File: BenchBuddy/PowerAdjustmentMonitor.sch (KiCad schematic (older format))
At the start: 0 parts

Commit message: Week3 Part 2
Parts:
- added JP? (x3): JUMPER, ~, symbol JUMPER
- added R? (x8): R, ~, symbol R
- added R? (x2): RVAR, ~, symbol RVAR
- added U? (x2): LM317, ~, symbol LM317
- added U? (x2): 7805, ~, symbol 7805
- added U? (x2): LM324, symbol LM324
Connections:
- new net: R?.1, R?.2, U?.2 (ADJ)
- new net: R?.2, R?.2, U?.2 (ADJ)
- new net +12V: U?.1 (IN), U?.4 (V+), U?.4 (V+), U?.VI
- new net -12V: JP?.2, U?.1 (IN), U?.11 (V-), U?.11 (V-), U?.VI
- new net AGND: JP?.2, R?.1, R?.1, R?.1, R?.2, U?.GND, U?.GND
- new net FE_V+: JP?.2, U?.VO
- new net FE_V-: JP?.1, U?.VO
- new net GND: JP?.1
- new net V+_ADJ: R?.1, R?.2
- new net V+_ADJ_MON: R?.1, R?.2
- new net V+_CURR_MON: U?.1, U?.2 (-)
- new net V+_MON: R?.1, R?.1, U?.3 (+), U?.3 (OUT)
- new net V-_ADJ: R?.2, R?.2
- new net V-_ADJ_MON: R?.1, R?.2
- new net V-_CURR_MON: U?.1, U?.2 (-)
- new net V-_MON: R?.1, R?.2, U?.3 (+), U?.3 (OUT)

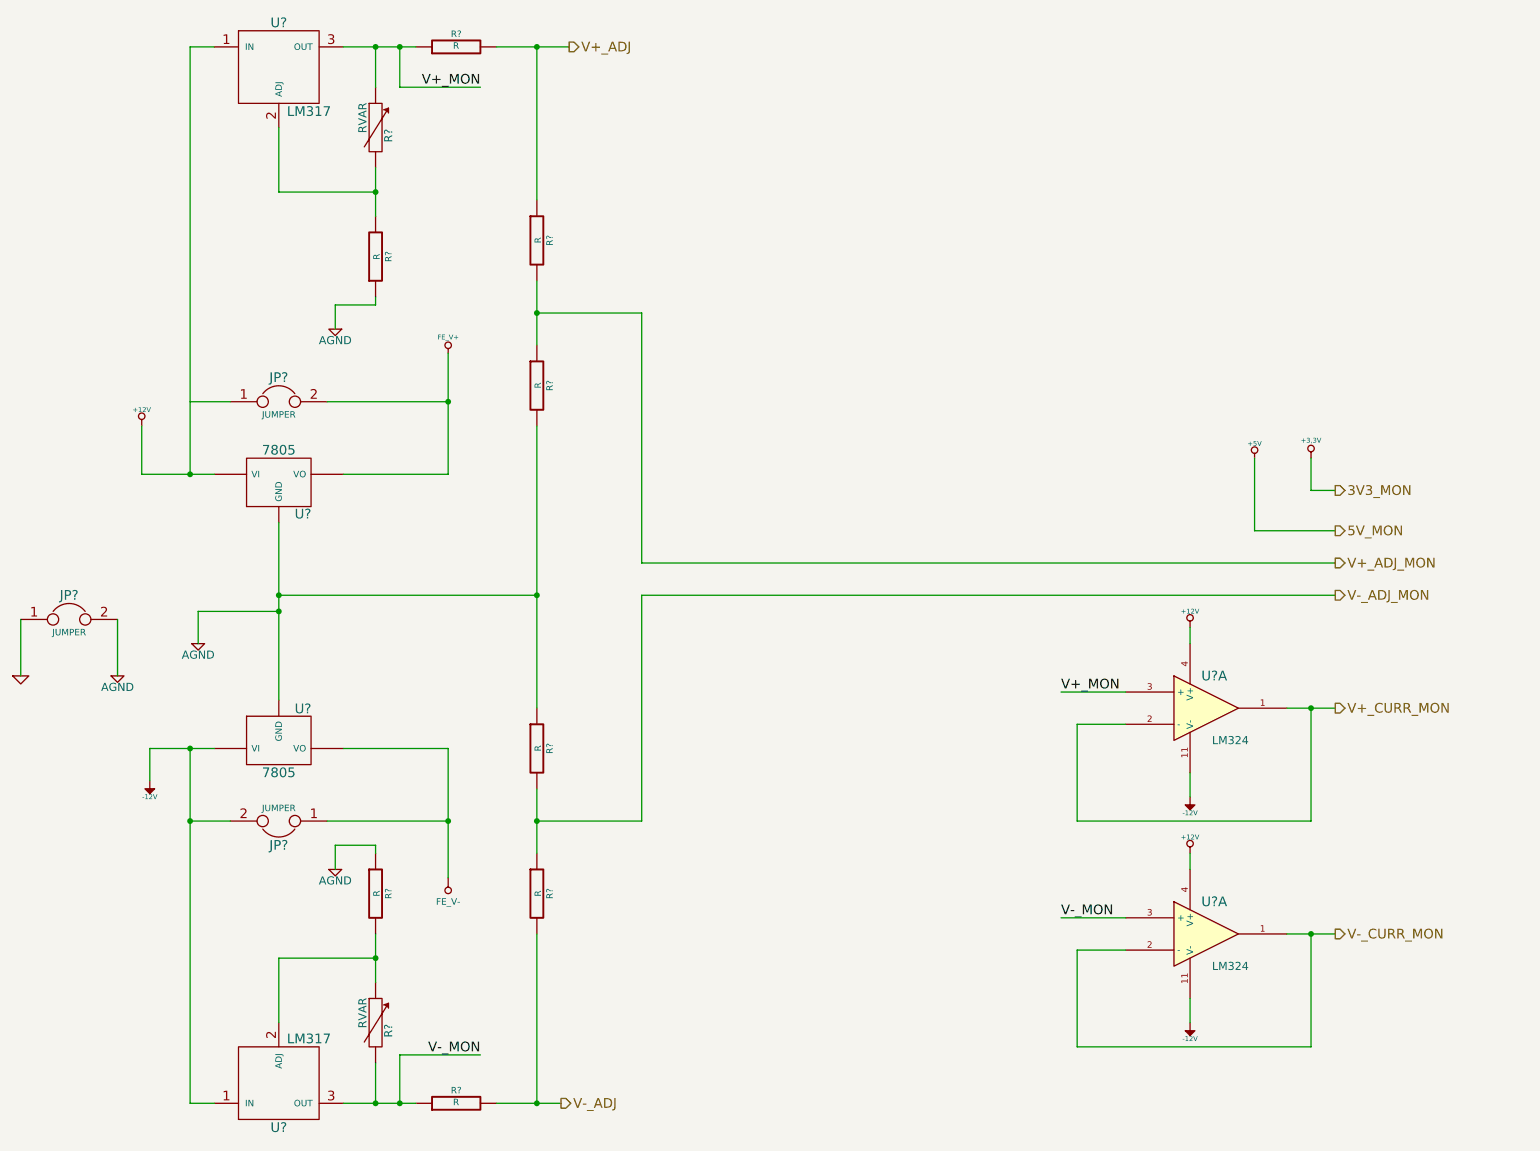
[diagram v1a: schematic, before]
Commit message: Colocação dos Componentes Relé
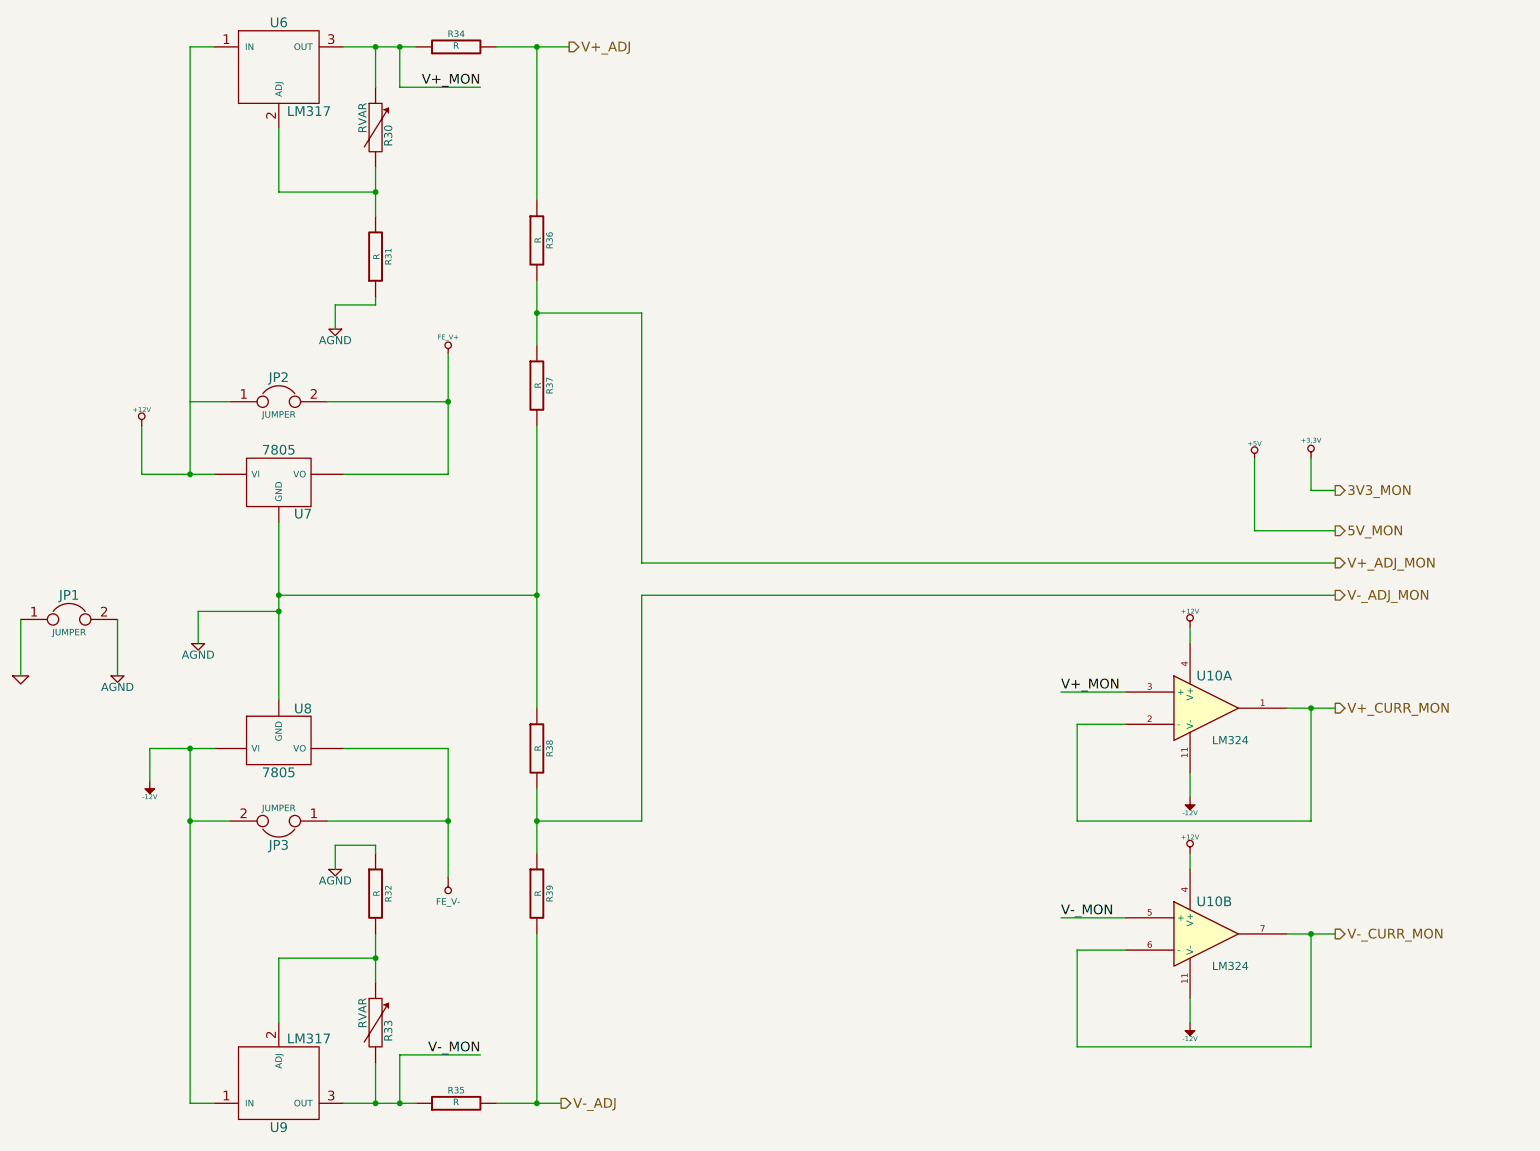
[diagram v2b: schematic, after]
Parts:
- gave numbers to parts that had none: 18
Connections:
- net V-_CURR_MON: now also U10.6 (-), U10.7; no longer U10.1, U10.2 (-)
- net V-_MON: now also U10.5 (+); no longer U10.3 (+)
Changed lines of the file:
@@
 Sheet 6 9
 Title ""
-Date "7 mar 2014"
+Date "9 mar 2014"
 Rev ""
 Comp ""
@@
 $EndDescr
 $Comp
-L +3,3V #PWR?
+L +3,3V #PWR44
 U 1 1 531776F8
 P 9050 3500
-F 0 "#PWR?" H 9050 3460 30  0001 C CNN
+F 0 "#PWR44" H 9050 3460 30  0001 C CNN
 F 1 "+3,3V" H 9050 3610 30  0000 C CNN
 F 2 "" H 9050 3500 60  0000 C CNN
@@
 $EndComp
 $Comp
-L +5V #PWR?
+L +5V #PWR43
 U 1 1 531776FE
 P 8700 3500
-F 0 "#PWR?" H 8700 3590 20  0001 C CNN
+F 0 "#PWR43" H 8700 3590 20  0001 C CNN
 F 1 "+5V" H 8700 3590 30  0000 C CNN
 F 2 "" H 8700 3500 60  0000 C CNN
@@
 $EndComp
 $Comp
-L +12V #PWR?
+L +12V #PWR32
 U 1 1 5317778A
 P 1800 3300
-F 0 "#PWR?" H 1800 3250 20  0001 C CNN
+F 0 "#PWR32" H 1800 3250 20  0001 C CNN
 F 1 "+12V" H 1800 3400 30  0000 C CNN
 F 2 "" H 1800 3300 60  0000 C CNN
@@
 $EndComp
 $Comp
-L -12V #PWR?
+L -12V #PWR33
 U 1 1 53177790
 P 1850 5500
-F 0 "#PWR?" H 1850 5630 20  0001 C CNN
+F 0 "#PWR33" H 1850 5630 20  0001 C CNN
 F 1 "-12V" H 1850 5600 30  0000 C CNN
 F 2 "" H 1850 5500 60  0000 C CNN
@@
 $EndComp
 $Comp
-L LM317 U?
+L LM317 U9
 U 1 1 531777B3
 P 2650 7350
-F 0 "U?" H 2650 7650 60  0000 C CNN
+F 0 "U9" H 2650 7650 60  0000 C CNN
 F 1 "LM317" H 2700 7100 60  0000 L CNN
 F 2 "~" H 2650 7350 60  0000 C CNN
@@
 	1850 5300 1850 5500
 $Comp
-L JUMPER JP?
+L JUMPER JP2
 U 1 1 531777D1
 P 2650 3150
-F 0 "JP?" H 2650 3300 60  0000 C CNN
+F 0 "JP2" H 2650 3300 60  0000 C CNN
 F 1 "JUMPER" H 2650 3070 40  0000 C CNN
 F 2 "~" H 2650 3150 60  0000 C CNN
@@
 $EndComp
 $Comp
-L JUMPER JP?
+L JUMPER JP3
 U 1 1 531777DE
 P 2650 5750
-F 0 "JP?" H 2650 5900 60  0000 C CNN
+F 0 "JP3" H 2650 5900 60  0000 C CNN
 F 1 "JUMPER" H 2650 5670 40  0000 C CNN
 F 2 "~" H 2650 5750 60  0000 C CNN
@@
 Connection ~ 2650 4450
 $Comp
-L JUMPER JP?
+L JUMPER JP1
 U 1 1 53177825
 P 1350 4500
-F 0 "JP?" H 1350 4650 60  0000 C CNN
+F 0 "JP1" H 1350 4650 60  0000 C CNN
 F 1 "JUMPER" H 1350 4420 40  0000 C CNN
 F 2 "~" H 1350 4500 60  0000 C CNN
@@
 $EndComp
 $Comp
-L AGND #PWR?
+L AGND #PWR31
 U 1 1 5317782D
 P 1650 4850
-F 0 "#PWR?" H 1650 4850 40  0001 C CNN
+F 0 "#PWR31" H 1650 4850 40  0001 C CNN
 F 1 "AGND" H 1650 4780 50  0000 C CNN
 F 2 "~" H 1650 4850 60  0000 C CNN
@@
 $EndComp
 $Comp
-L GND #PWR?
+L GND #PWR30
 U 1 1 5317783C
 P 1050 4850
-F 0 "#PWR?" H 1050 4850 30  0001 C CNN
+F 0 "#PWR30" H 1050 4850 30  0001 C CNN
 F 1 "GND" H 1050 4780 30  0001 C CNN
 F 2 "~" H 1050 4850 60  0000 C CNN
@@
 	1650 4500 1650 4850
 $Comp
-L AGND #PWR?
+L AGND #PWR34
 U 1 1 53177892
 P 2150 4650
-F 0 "#PWR?" H 2150 4650 40  0001 C CNN
+F 0 "#PWR34" H 2150 4650 40  0001 C CNN
 F 1 "AGND" H 2150 4580 50  0000 C CNN
 F 2 "~" H 2150 4650 60  0000 C CNN
@@
 $EndComp
 $Comp
-L FE_V+ #PWR?
+L FE_V+ #PWR37
 U 1 1 53177BD8
 P 3700 2850
-F 0 "#PWR?" H 3700 2950 30  0001 C CNN
+F 0 "#PWR37" H 3700 2950 30  0001 C CNN
 F 1 "FE_V+" H 3700 2950 30  0000 C CNN
 F 2 "~" H 3700 2850 60  0000 C CNN
@@
 $EndComp
 $Comp
-L FE_V- #PWR?
+L FE_V- #PWR38
 U 1 1 53177BE7
 P 3700 6100
-F 0 "#PWR?" H 3700 6300 40  0001 C CNN
+F 0 "#PWR38" H 3700 6300 40  0001 C CNN
 F 1 "FE_V-" H 3700 6250 40  0000 C CNN
 F 2 "~" H 3700 6100 60  0000 C CNN
@@
 $EndComp
 $Comp
-L 7805 U?
+L 7805 U7
 U 1 1 53177C4D
 P 2650 3650
-F 0 "U?" H 2800 3454 60  0000 C CNN
+F 0 "U7" H 2800 3454 60  0000 C CNN
 F 1 "7805" H 2650 3850 60  0000 C CNN
 F 2 "~" H 2650 3650 60  0000 C CNN
@@
 $EndComp
 $Comp
-L 7805 U?
+L 7805 U8
 U 1 1 53177C64
 P 2650 5250
-F 0 "U?" H 2800 5054 60  0000 C CNN
+F 0 "U8" H 2800 5054 60  0000 C CNN
 F 1 "7805" H 2650 5450 60  0000 C CNN
 F 2 "~" H 2650 5250 60  0000 C CNN
@@
 Connection ~ 3700 5750
 $Comp
-L R R?
+L R R32
 U 1 1 53177DDD
 P 3250 6200
-F 0 "R?" V 3330 6200 40  0000 C CNN
+F 0 "R32" V 3330 6200 40  0000 C CNN
 F 1 "R" V 3257 6201 40  0000 C CNN
 F 2 "~" V 3180 6200 30  0000 C CNN
@@
 Connection ~ 3250 6600
 $Comp
-L AGND #PWR?
+L AGND #PWR36
 U 1 1 53177E7E
 P 3000 6050
-F 0 "#PWR?" H 3000 6050 40  0001 C CNN
+F 0 "#PWR36" H 3000 6050 40  0001 C CNN
 F 1 "AGND" H 3000 5980 50  0000 C CNN
 F 2 "~" H 3000 6050 60  0000 C CNN
@@
 	3000 5900 3000 6050
 $Comp
-L LM317 U?
+L LM317 U6
 U 1 1 53177EB1
 P 2650 1100
-F 0 "U?" H 2650 1400 60  0000 C CNN
+F 0 "U6" H 2650 1400 60  0000 C CNN
 F 1 "LM317" H 2700 850 60  0000 L CNN
 F 2 "~" H 2650 1100 60  0000 C CNN
@@
 	2100 950  2250 950
 $Comp
-L R R?
+L R R31
 U 1 1 53177EBF
 P 3250 2250
-F 0 "R?" V 3330 2250 40  0000 C CNN
+F 0 "R31" V 3330 2250 40  0000 C CNN
 F 1 "R" V 3257 2251 40  0000 C CNN
 F 2 "~" V 3180 2250 30  0000 C CNN
@@
 Connection ~ 3250 1850
 $Comp
-L AGND #PWR?
+L AGND #PWR35
 U 1 1 53177ECC
 P 3000 2700
-F 0 "#PWR?" H 3000 2700 40  0001 C CNN
+F 0 "#PWR35" H 3000 2700 40  0001 C CNN
 F 1 "AGND" H 3000 2630 50  0000 C CNN
 F 2 "~" H 3000 2700 60  0000 C CNN
@@
 V-_CURR_MON
 $Comp
-L R R?
+L R R36
 U 1 1 53178157
 P 4250 2150
-F 0 "R?" V 4330 2150 40  0000 C CNN
+F 0 "R36" V 4330 2150 40  0000 C CNN
 F 1 "R" V 4257 2151 40  0000 C CNN
 F 2 "~" V 4180 2150 30  0000 C CNN
@@
 $EndComp
 $Comp
-L R R?
+L R R37
 U 1 1 53178166
 P 4250 3050
-F 0 "R?" V 4330 3050 40  0000 C CNN
+F 0 "R37" V 4330 3050 40  0000 C CNN
 F 1 "R" V 4257 3051 40  0000 C CNN
 F 2 "~" V 4180 3050 30  0000 C CNN
@@
 Connection ~ 2650 4350
 $Comp
-L R R?
+L R R38
 U 1 1 5317820A
 P 4250 5300
-F 0 "R?" V 4330 5300 40  0000 C CNN
+F 0 "R38" V 4330 5300 40  0000 C CNN
 F 1 "R" V 4257 5301 40  0000 C CNN
 F 2 "~" V 4180 5300 30  0000 C CNN
@@
 $EndComp
 $Comp
-L R R?
+L R R39
 U 1 1 53178210
 P 4250 6200
-F 0 "R?" V 4330 6200 40  0000 C CNN
+F 0 "R39" V 4330 6200 40  0000 C CNN
 F 1 "R" V 4257 6201 40  0000 C CNN
 F 2 "~" V 4180 6200 30  0000 C CNN
@@
 	9050 3700 9200 3700
 $Comp
-L R R?
+L R R35
 U 1 1 531783D8
 P 3750 7500
-F 0 "R?" V 3830 7500 40  0000 C CNN
+F 0 "R35" V 3830 7500 40  0000 C CNN
 F 1 "R" V 3757 7501 40  0000 C CNN
 F 2 "~" V 3680 7500 30  0000 C CNN
@@
 $EndComp
 $Comp
-L R R?
+L R R34
 U 1 1 531783DE
 P 3750 950
-F 0 "R?" V 3830 950 40  0000 C CNN
+F 0 "R34" V 3830 950 40  0000 C CNN
 F 1 "R" V 3757 951 40  0000 C CNN
 F 2 "~" V 3680 950 30  0000 C CNN
@@
 	4900 2600 4900 4150
 $Comp
-L LM324 U?
-U 1 1 5317946A
+L LM324 U10
+U 2 1 5317946A
 P 8400 6450
-F 0 "U?" H 8450 6650 60  0000 C CNN
+F 0 "U10" H 8450 6650 60  0000 C CNN
 F 1 "LM324" H 8550 6250 50  0000 C CNN
 F 2 "" H 8400 6450 60  0000 C CNN
 F 3 "" H 8400 6450 60  0000 C CNN
-	1    8400 6450
-	1    0    0    -1
-$EndComp
-$Comp
-L +12V #PWR?
+	2    8400 6450
+	1    0    0    -1
+$EndComp
+$Comp
+L +12V #PWR41
 U 1 1 53179470
 P 8300 5950
-F 0 "#PWR?" H 8300 5900 20  0001 C CNN
+F 0 "#PWR41" H 8300 5900 20  0001 C CNN
 F 1 "+12V" H 8300 6050 30  0000 C CNN
 F 2 "" H 8300 5950 60  0000 C CNN
@@
 $EndComp
 $Comp
-L -12V #PWR?
+L -12V #PWR42
 U 1 1 53179480
 P 8300 7000
-F 0 "#PWR?" H 8300 7130 20  0001 C CNN
+F 0 "#PWR42" H 8300 7130 20  0001 C CNN
 F 1 "-12V" H 8300 7100 30  0000 C CNN
 F 2 "" H 8300 7000 60  0000 C CNN
@@
 	8300 6850 8300 7000
 $Comp
-L LM324 U?
+L LM324 U10
 U 1 1 53179548
 P 8400 5050
-F 0 "U?" H 8450 5250 60  0000 C CNN
+F 0 "U10" H 8450 5250 60  0000 C CNN
 F 1 "LM324" H 8550 4850 50  0000 C CNN
 F 2 "" H 8400 5050 60  0000 C CNN
@@
 $EndComp
 $Comp
-L +12V #PWR?
+L +12V #PWR39
 U 1 1 5317954E
 P 8300 4550
-F 0 "#PWR?" H 8300 4500 20  0001 C CNN
+F 0 "#PWR39" H 8300 4500 20  0001 C CNN
 F 1 "+12V" H 8300 4650 30  0000 C CNN
 F 2 "" H 8300 4550 60  0000 C CNN
@@
 $EndComp
 $Comp
-L -12V #PWR?
+L -12V #PWR40
 U 1 1 53179554
 P 8300 5600
-F 0 "#PWR?" H 8300 5730 20  0001 C CNN
+F 0 "#PWR40" H 8300 5730 20  0001 C CNN
 F 1 "-12V" H 8300 5700 30  0000 C CNN
 F 2 "" H 8300 5600 60  0000 C CNN
@@
 V+_MON
 $Comp
-L RVAR R?
+L RVAR R33
 U 1 1 5317987C
 P 3250 7000
-F 0 "R?" V 3330 6950 50  0000 C CNN
+F 0 "R33" V 3330 6950 50  0000 C CNN
 F 1 "RVAR" V 3170 7060 50  0000 C CNN
 F 2 "~" H 3250 7000 60  0000 C CNN
@@
 $EndComp
 $Comp
-L RVAR R?
+L RVAR R30
 U 1 1 531798F3
 P 3250 1450
-F 0 "R?" V 3330 1400 50  0000 C CNN
+F 0 "R30" V 3330 1400 50  0000 C CNN
 F 1 "RVAR" V 3170 1510 50  0000 C CNN
 F 2 "~" H 3250 1450 60  0000 C CNN

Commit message: Pre layout
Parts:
- removed JP1, JP2, JP3: JUMPER, ~, symbol JUMPER
- removed R34, R35: R, ~, symbol R
- removed U10: LM324, symbol LM324
- removed U7, U8: 7805, ~, symbol 7805
- added C14, C15, C16, C17, C18, C19, C20, C21, C22, C23, C24, C25: C, ~, symbol C
- added D10, D11, D12, D3, D6, D7, D8, D9: MMBD914-7F, ~, symbol DIODE
- added R54, R55, R56, R57: R, ~, symbol R
- added U7, U8: LM337T, TO-220, symbol LM337T
- R30, R33: value RVAR -> 5k
- R31, R32: value R -> 715
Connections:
- net +12V: now also U9.1 (IN), C15.1, C17.1, D6.2 (K), D8.2 (K)
- net -12V: now also C14.2, C16.2, D3.2 (K), D7.2 (K), U7.2 (IN), U8.2 (IN); no longer U9.1 (IN)
- net AGND: now also C16.1, C17.2, C20.2, C21.1, C23.1, C25.2, R54.2, R57.1; no longer R31.1, R32.1, R37.2, R38.1
- net FE_V+: now also U9.3 (OUT), C25.1, D11.2 (K), D8.1 (A), R56.2
- net FE_V-: now also C23.2, D10.1 (A), D7.1 (A), R55.1, U8.3 (OUT)
- net V+_ADJ: now also R31.2, U6.3 (OUT), C24.1, D12.2 (K), D6.1 (A)
- net V-_ADJ: now also R32.1, C22.2, D3.1 (A), D9.1 (A), U7.3 (OUT)
- net V+_MON: no longer names the net of R30.1
- net V+_MON: now also R31.1, U6.2 (ADJ), C19.1, D12.1 (A); no longer U6.3 (OUT)
- net V-_MON: no longer names the net of R33.2
- net V-_MON: now also R32.2, C18.2, D9.2 (K), U7.1 (ADJ); no longer U9.3 (OUT)
- new net: C20.1, D11.1 (A), R56.1, R57.2, U9.2 (ADJ)
- new net: C21.2, D10.2 (K), R54.1, R55.2, U8.1 (ADJ)
- new net GND_PWR: C14.1, C15.2, C18.1, C19.2, C22.1, C24.2, R30.2, R33.1, R37.2, R38.1
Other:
- note added: "-1,5V to -10V Outrput"
- note added: "-10V Output"
- note added: "1,5V to 10V Outrput"
- note added: "10V Output"
- moved on the sheet: R30, R31, R36, R37, R38, R39, U6
